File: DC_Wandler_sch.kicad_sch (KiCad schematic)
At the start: 60 parts, among them IC1 ICE2PCS02GXUMA1, Q1/Thermalposition STP22NM60N, Q1/Thermalposition1 STP22NM60N, U1 NCP1246BD065R2G, U2 PC817XNNIP1B, U3 TL431

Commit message: Add files via upload
Change Diode TL431
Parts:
- U3: Typ (none) -> Nexperia TL431IDBZR
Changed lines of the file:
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@@
 			)
 		)
-		(property "Typ" ""
+		(property "Typ" "Nexperia TL431IDBZR"
 			(at 256.54 149.86 90)
 			(effects

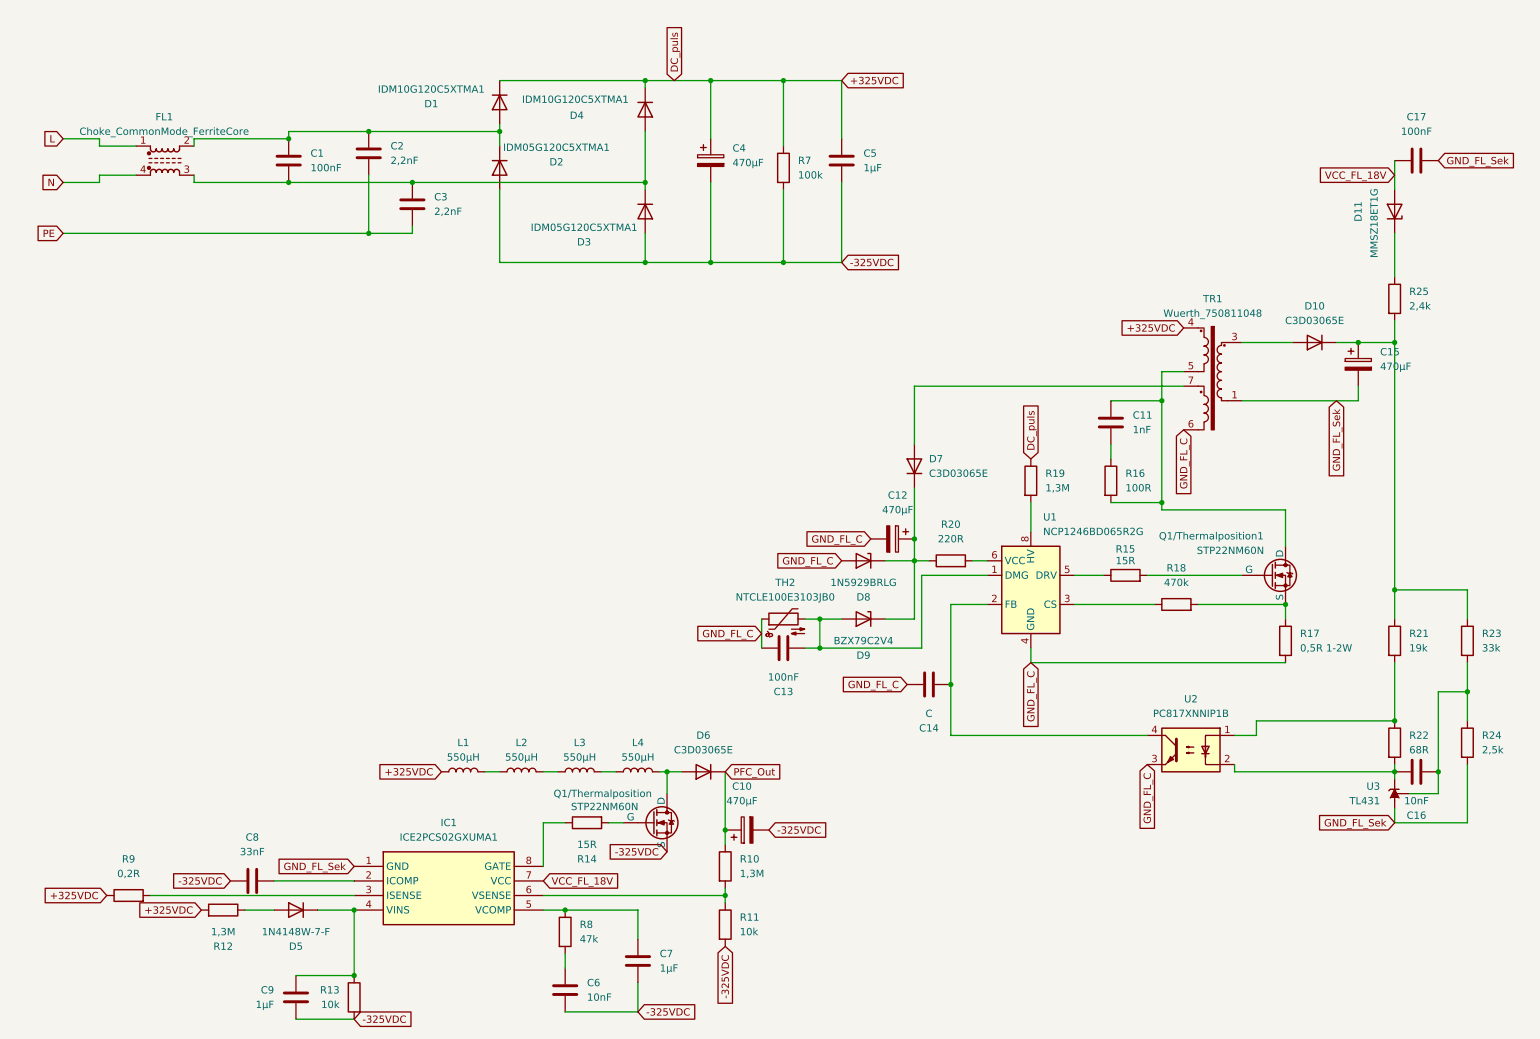
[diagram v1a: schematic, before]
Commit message: ESP32 Supply gestartet
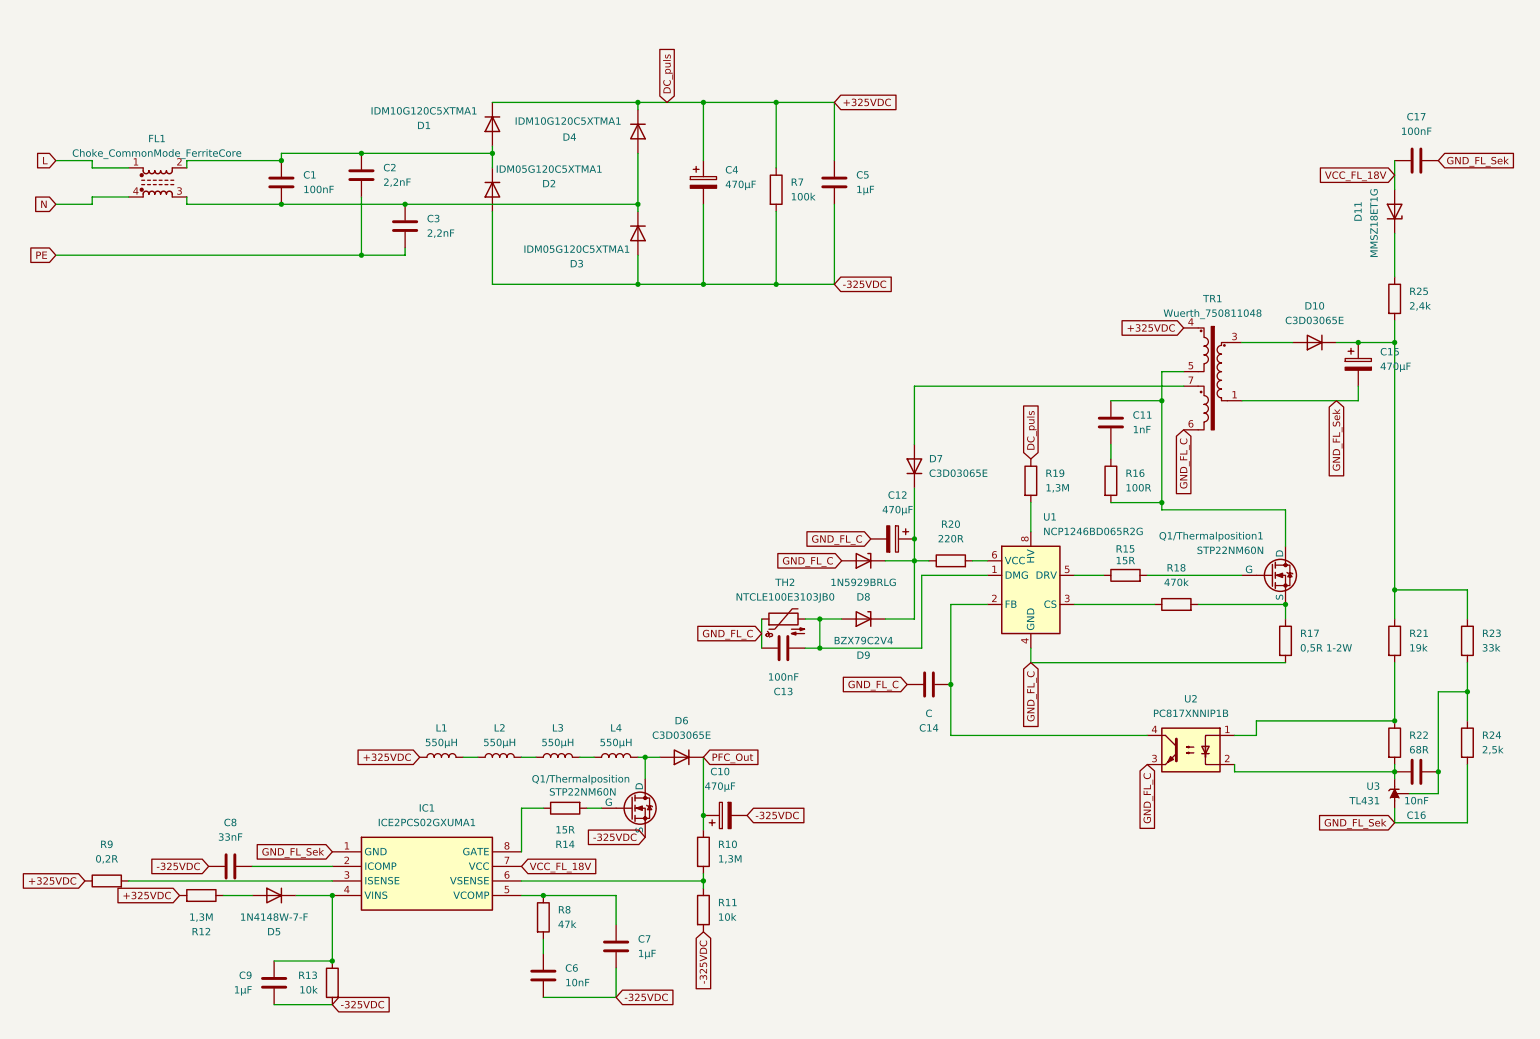
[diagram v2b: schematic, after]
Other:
- moved on the sheet: C1, C10, C2, C3, C4, C5, C6, C7, C8, C9, D1, D2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
